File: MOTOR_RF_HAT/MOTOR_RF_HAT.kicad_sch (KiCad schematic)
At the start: 0 parts

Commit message: MOTOR_RF_HAT: port full RF_HAT project with all libs localized
Copied complete RF_HAT_out KiCad project (schematic + PCB layout +
4 hierarchical sub-sheets) as the base for the combined board.

Changes from original RF_HAT:
- Renamed RF_HAT → MOTOR_RF_HAT in all project/schematic references
- Imported LMR51420YDDCR + XRTC303020D4R7MBCA symbols from personal
  lib into project-local components.kicad_sym
- Copied corresponding footprints + 3D models (SOT-23-6, inductor)
  into components.pretty/ and components.3dshapes/
- Fixed all lib: → components: references in schematics and PCB
- Removed reference/ directory (schematics are now live sub-sheets)
- ERC: 20 violations (19 pre-existing from RF_HAT + 1 from rename)
- Zero external library dependencies — fully self-contained

Ready to add motor driver (A4950E), encoder, and IMU (ADXL345)
sub-sheets. Existing CC1200 UHF/VHF, Pi header, Pico, power,
NeoPixel, and buzzer circuits carry over unchanged.

Co-Authored-By: Claude Opus 4.6 (1M context) <noreply@anthropic.com>
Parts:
- added C19: 4.7uF 50v, Capacitor_SMD:C_0805_2012Metric, symbol Device:C
- added C22: 100n, Capacitor_SMD:C_0603_1608Metric, symbol Device:C
- added C24: 22uF, Capacitor_SMD:C_0603_1608Metric, symbol Device:C
- added C48, C49, C50, C51: 220nF, Capacitor_SMD:C_0603_1608Metric, symbol Device:C
- added D1: D_Schottky, Diode_SMD:D_0603_1608Metric, symbol Device:D_Schottky
- added D2: 1N4148WS, Diode_SMD:D_SOD-323, symbol Diode:1N4148WS
- added D3, D4, D5, D6: WS2812B-2020, LED_SMD:LED_WS2812B-2020_PLCC4_2.0x2.0mm, symbol LED:WS2812B-2020
- added H1, H4: MountingHole_Pad, MountingHole:MountingHole_2.7mm_M2.5_ISO7380_Pad, symbol Mechanical:MountingHole_Pad
- added J4, J5: Conn_01x01, Connector_PinHeader_2.00mm:PinHeader_1x01_P2.00mm_Vertical, symbol Connector_Generic:Conn_01x01
- added L18: XRTC303020D4R7MBCA, components:IND-SMD_L3.0-W3.0_AFE303020S, symbol components:XRTC303020D4R7MBCA
- added Q1: BSS138, Package_TO_SOT_SMD:SOT-23, symbol Transistor_FET:BSS138
- added R16: 100k, Capacitor_SMD:C_0603_1608Metric, symbol Device:R
- added R17: 13.7k, Capacitor_SMD:C_0603_1608Metric, symbol Device:R
- added U4: XT30PW-M, Connector_AMASS:AMASS_XT30PW-M_1x02_P2.50mm_Horizontal, symbol components:XT30PW-M
- added U5: LMR51420YFDDCR, components:SOT-23-6_L2.9-W1.6-P0.95-LS2.9-BL, symbol components:LMR51420YDDCR
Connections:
- new net: R16.1, R17.1, U5.4 (FB)
- new net: D5.1 (DOUT), D6.3 (DIN)
- new net: D4.1 (DOUT), D5.3 (DIN)
- new net: D3.1 (DOUT), D4.3 (DIN)
- new net: D2.2 (A), J5.1 (Pin_1), Q1.3 (D)
- new net: C22.1, L18.1, U5.2 (SW)
- new net: C22.2, U5.6 (CB)
- new net +24V: C19.1, U4.2 (+), U5.3 (VIN), U5.5 (EN)
- new net +3V3: C48.1, C49.1, C50.1, C51.1, D2.1 (K), D3.4 (VDD), D4.4 (VDD), D5.4 (VDD), D6.4 (VDD), J4.1 (Pin_1)
- new net +5V: D1.1 (K)
- new net +5V_BUCK: C24.1, D1.2 (A), L18.2, R16.2
- new net GND: C19.2, C24.2, C48.2, C49.2, C50.2, C51.2, D3.2 (VSS), D4.2 (VSS), D5.2 (VSS), D6.2 (VSS), H1.1, H4.1, Q1.2 (S), R17.2, U4.1 (-), U5.1 (GND)
- new net Pico_SPI_Host/BUZZER: Q1.1 (G)
- new net WS2812B: D3.3 (DIN)
- no-connect marks 0 -> 3
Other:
- added sheet CC1200_UHF_432MHz (CC1200_UHF_432MHz.kicad_sch)
- added sheet CC1200_VHF_144MHz (CC1200_VHF_144MHz.kicad_sch)
- added sheet Pi_Header (Pi_Header.kicad_sch)
- added sheet Pico_SPI_Host (Pico_SPI_Host.kicad_sch)
- note added: "5V (2A)"
- note added: "FPWM version of the LMR51420YFDDCR for less output ripple at low voltage and more consistency but less efficient"
- company: SatNOGS Basestation — Stan Coene & Robbe Lehaen -> (none)
- title: MOTOR_RF_HAT — Combined Motor Control + RF HAT -> MOTOR_RF_HAT

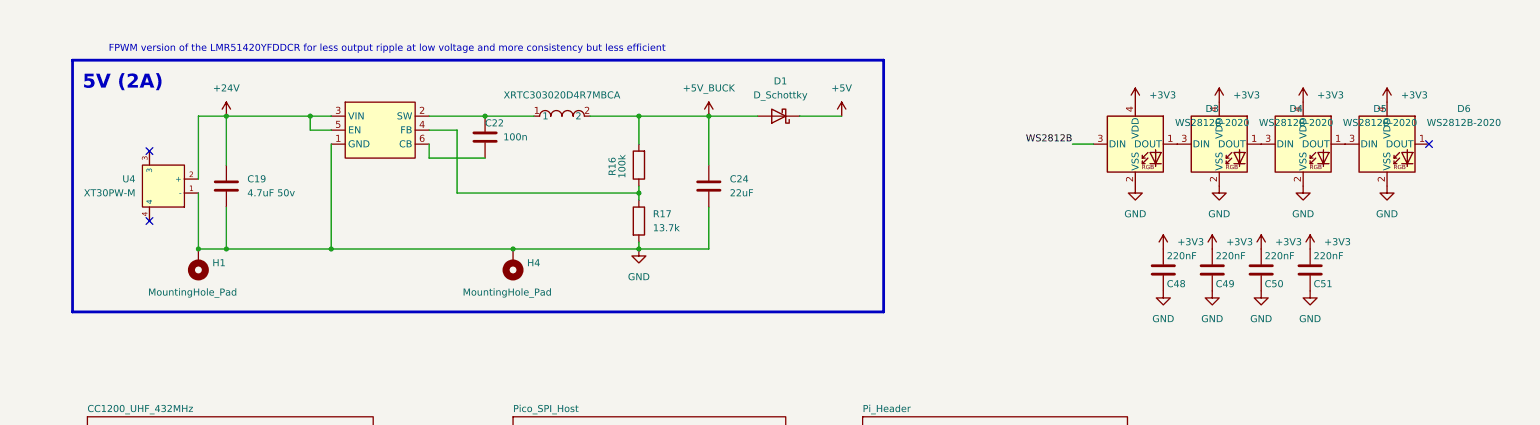
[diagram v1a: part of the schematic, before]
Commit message: MOTOR_RF_HAT: pin library, remove on-board ADXL345
- Pinned 'components' in both symbol and footprint choosers
  (shows starred at top of library browser)
- Removed ADXL345 symbol and LGA-14 footprint — IMU connects
  via solder pads to external breakout (same as MotorPCB)
- Use Connector:TestPoint_Small for IMU solder pads (KiCad global)
- Kept ADXL345 datasheet for wiring reference

Co-Authored-By: Claude Opus 4.6 (1M context) <noreply@anthropic.com>
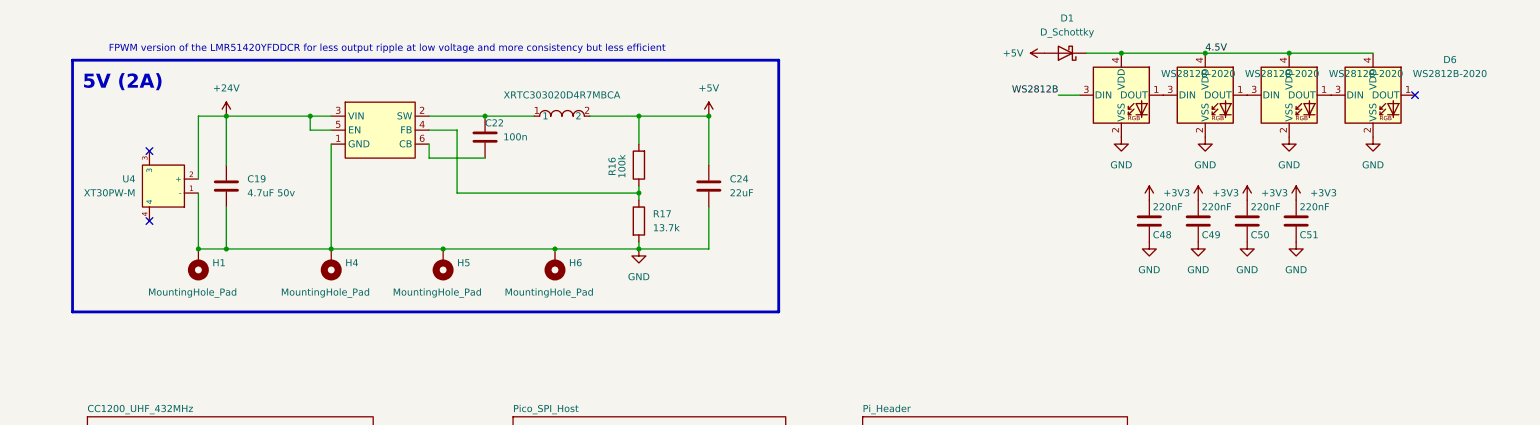
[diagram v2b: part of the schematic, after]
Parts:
- added H5, H6: MountingHole_Pad, MountingHole:MountingHole_2.7mm_M2.5_ISO7380_Pad, symbol Mechanical:MountingHole_Pad
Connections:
- net +5V_BUCK is gone; now on net +5V: C24.1, D1.2 (A), L18.2, R16.2
- net +3V3: no longer D3.4 (VDD), D4.4 (VDD), D5.4 (VDD), D6.4 (VDD)
- net +5V: no longer D1.1 (K)
- net GND: now also H5.1, H6.1
- new net 4.5V: D1.1 (K), D3.4 (VDD), D4.4 (VDD), D5.4 (VDD), D6.4 (VDD)
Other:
- moved on the sheet: C48, C49, C50, C51, D6, H4

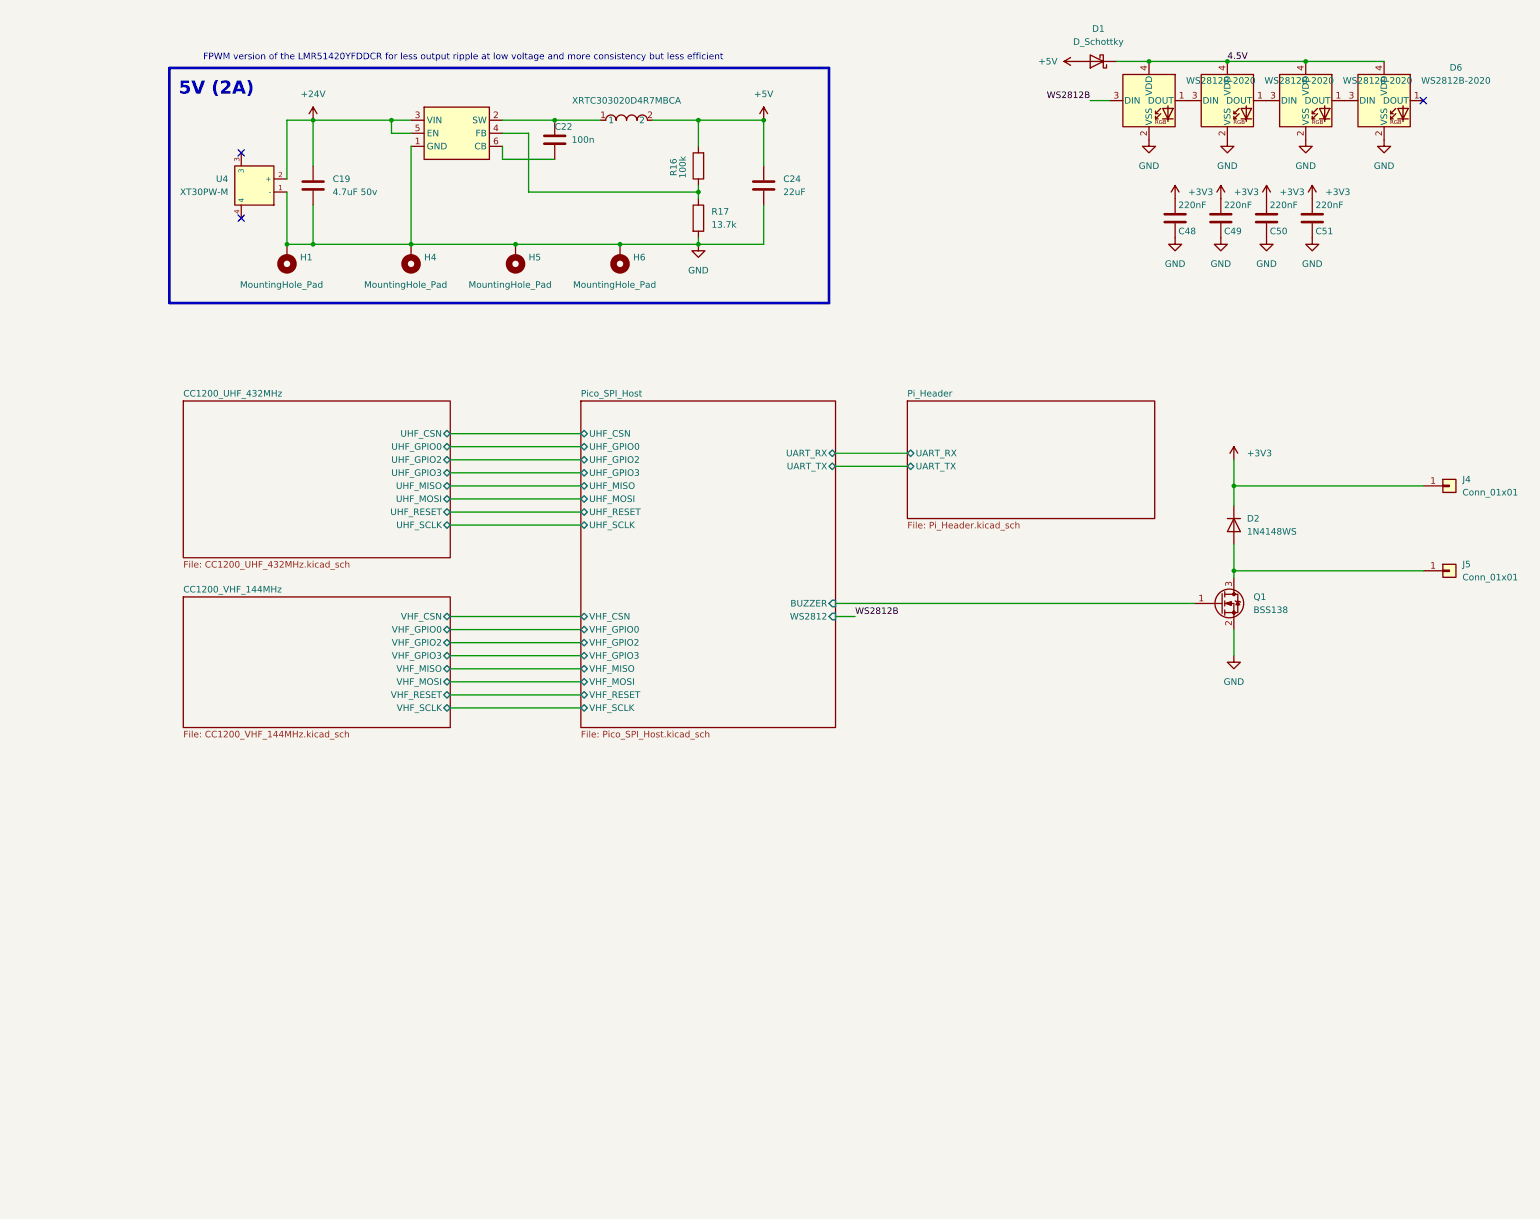
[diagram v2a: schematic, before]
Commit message: MOTOR_RF_HAT: link MotorPCB sub-sheets as hierarchical sheets
Added Encoders, Azimuth, Elevation, Gyro, and Solder_Pads as
hierarchical sheets in the root schematic. All sub-sheet files
are the actual MotorPCB originals with project refs updated.

Root schematic now has 9 sub-sheets:
- Pico_SPI_Host (from RF_HAT)
- CC1200_UHF_432MHz (from RF_HAT)
- CC1200_VHF_144MHz (from RF_HAT)
- Pi_Header (from RF_HAT)
- Encoders (from MotorPCB — 6-pin JST with motor + encoder)
- Azimuth (from MotorPCB — TB6642FG, to be replaced with A4950E)
- Elevation (from MotorPCB — TB6642FG, to be replaced with A4950E)
- Gyro (from MotorPCB — ADXL345 via solder pads)
- Solder_Pads (from MotorPCB — test points for SPI/UART/I2C)

ERC has 148 violations — expected: motor driver sheets still
reference easyeda2kicad:TB6642FG (needs manual swap to A4950E),
hierarchical pins not yet wired on root sheet, and pre-existing
MotorPCB ERC issues.

Co-Authored-By: Claude Opus 4.6 (1M context) <noreply@anthropic.com>
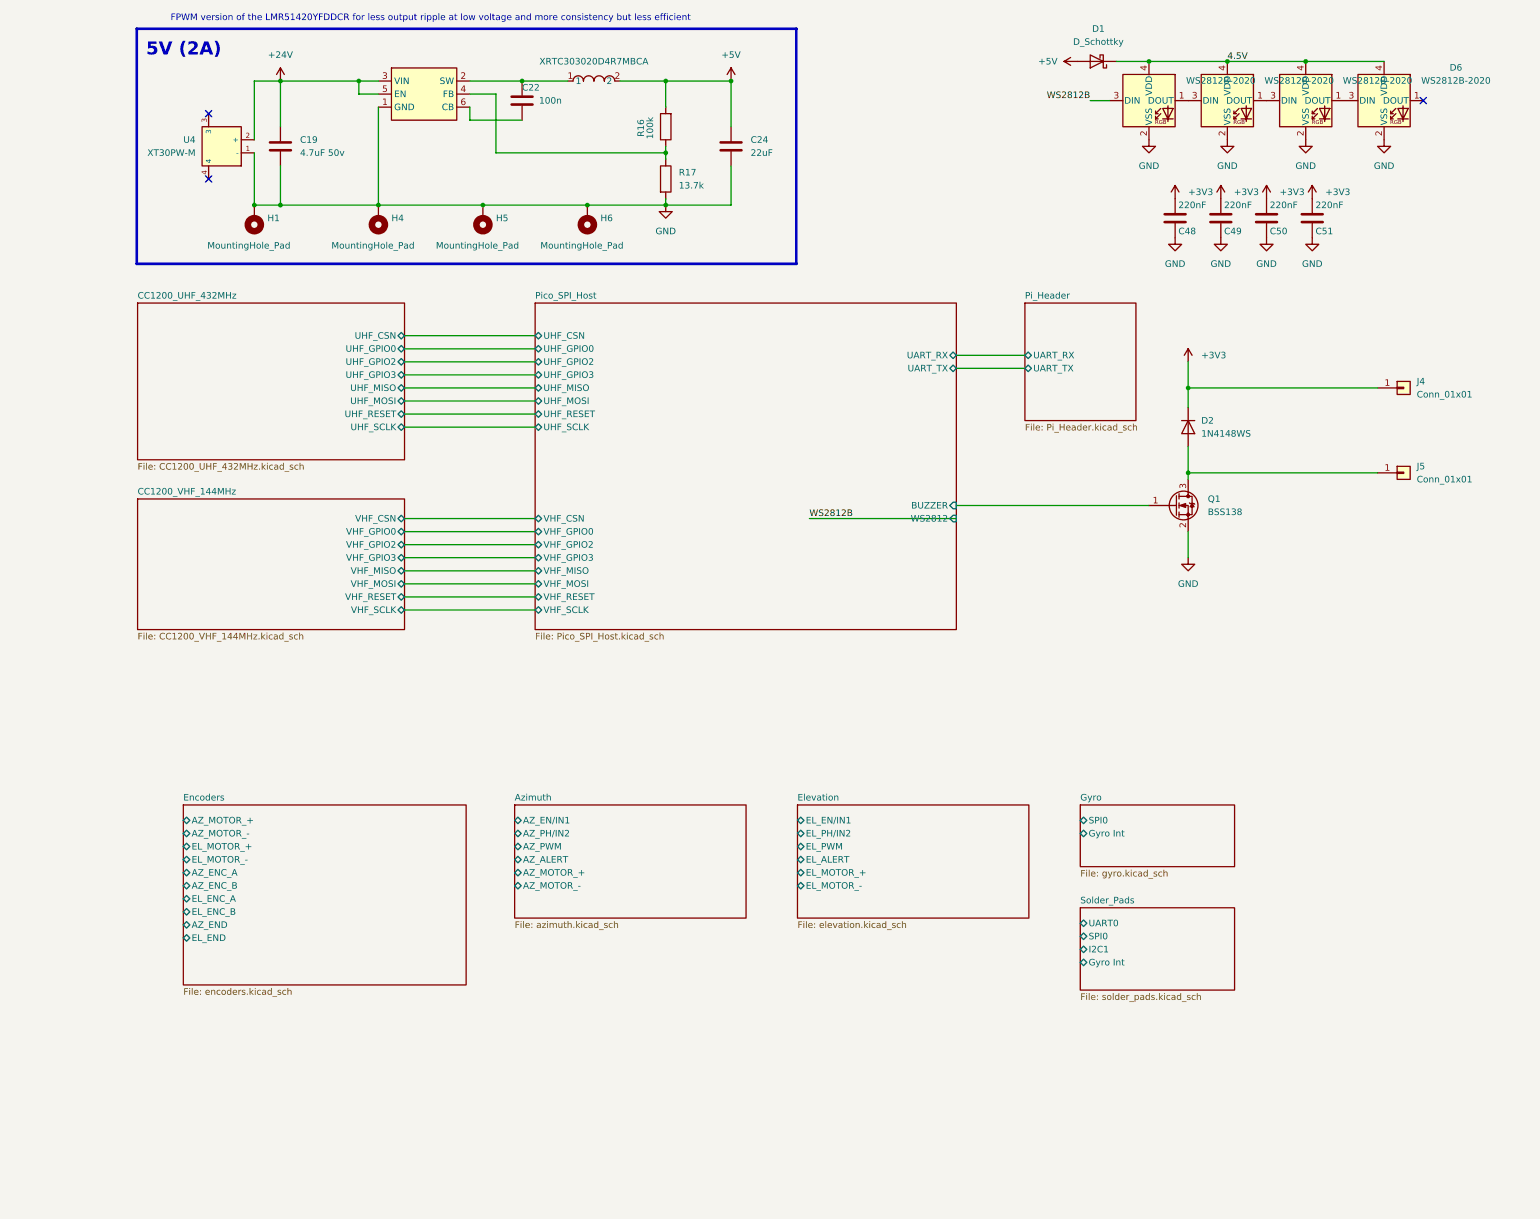
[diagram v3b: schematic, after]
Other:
- added sheet Azimuth (azimuth.kicad_sch)
- added sheet Elevation (elevation.kicad_sch)
- added sheet Encoders (encoders.kicad_sch)
- added sheet Gyro (gyro.kicad_sch)
- added sheet Solder_Pads (solder_pads.kicad_sch)
- moved on the sheet: C19, C22, C24, D2, H1, H4, H5, H6, J4, J5, Q1, R16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

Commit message: MOTOR_RF_HAT: assign components:smallpad to all TestPoint_Small
Assigned local smallpad footprint to 8 TestPoint_Small instances:
- 7 in solder_pads.kicad_sch
- 1 in root schematic (TP19)

Co-Authored-By: Claude Opus 4.6 (1M context) <noreply@anthropic.com>
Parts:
- added TP19: TestPoint_Small, components:smallpad, symbol Connector:TestPoint_Small
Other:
- note added: "add breakout pads"
